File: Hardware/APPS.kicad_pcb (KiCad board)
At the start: 2 copper layers, 100 x 63 mm, 83 parts, among them J1 Screw_Terminal_01x02, J2 Screw_Terminal_01x03, J3 Screw_Terminal_01x03, J4 Conn_01x06_Male, J5 Screw_Terminal_01x02, J6 Conn_01x06_Male, J7 Screw_Terminal_01x02, K1 FINDER-30.22, Q1 BSS138, SW1 SW_Push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

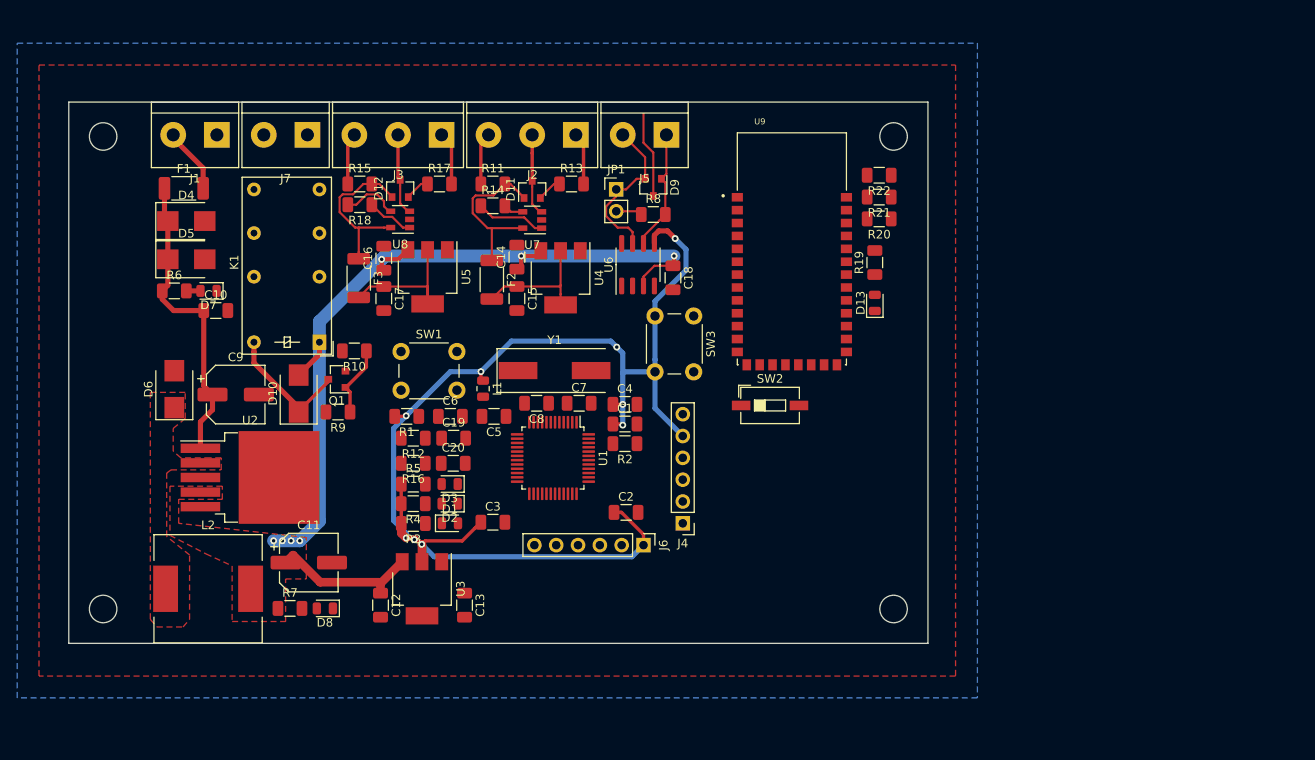
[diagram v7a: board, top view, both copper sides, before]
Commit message: Components labels placed
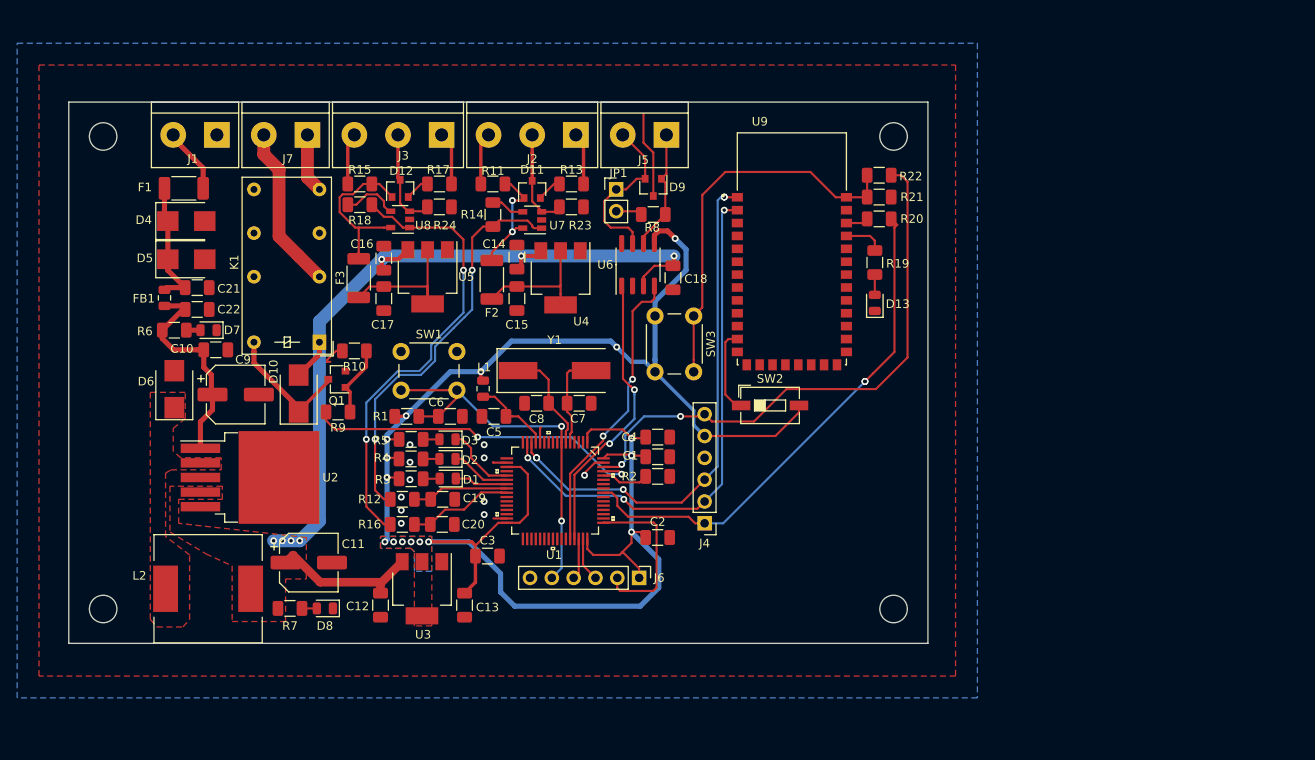
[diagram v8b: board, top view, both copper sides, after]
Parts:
- added C21: C_Small, Capacitor_SMD:C_1206_3216Metric, F.Cu at (87.0, 74.2)
- added C22: C_Small, Capacitor_SMD:C_1206_3216Metric, F.Cu at (87.0, 76.7)
- added FB1: Ferrite_Bead_Small, Inductor_SMD:L_0805_2012Metric, F.Cu at (83.2, 75.4)
- added R23: 100k, Resistor_SMD:R_1206_3216Metric, F.Cu at (130.6, 64.8)
- added R24: 100k, Resistor_SMD:R_1206_3216Metric, F.Cu at (115.2, 64.8)
- U1: value STM32F103C8Tx -> STM32L4P5RET6; footprint Package_QFP:LQFP-48_7x7mm_P0.5mm -> footprints:STM32L4P5RET6
- moved R16 7.22 mm to (110.9, 101.7)
- moved C19 7.22 mm to (115.6, 98.8)
- moved R12 7.22 mm to (110.9, 98.8)
- moved C20 7.22 mm to (115.5, 101.7)
- moved R2 5.39 mm to (140.6, 96.1)
- moved C1 5.39 mm to (140.6, 93.9)
- moved C4 5.39 mm to (140.6, 91.6)
- moved D3 5.21 mm to (116.1, 91.8)
- moved D1 5.21 mm to (116.2, 96.4), turned to 180 degrees
- moved D2 5.21 mm to (116.1, 94.1)
- moved R3 5.21 mm to (111.9, 96.4)
- moved R4 5.21 mm to (111.9, 94.1)
- moved R5 5.21 mm to (111.9, 91.8)
- moved C2 4.70 mm to (140.6, 103.3)
- moved C10 4.57 mm to (89.2, 81.4)
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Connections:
- C10 pad 1: +24V -> Net-(C10-Pad1)
- C9 pad 1: +24V -> Net-(C10-Pad1)
- R6 pad 1: +24V -> Net-(C10-Pad1)
- U1 pad 11: Ain0 -> Net-(U1-Pad11)
- U1 pad 12: Ain1 -> SW_GND
- U1 pad 13: Net-(U1-Pad13) -> 3V3_A
- U1 pad 14: Net-(U1-Pad14) -> BT_TX
- U1 pad 15: Led1 -> BT_RX
- U1 pad 16: Led2 -> Net-(U1-Pad16)
- U1 pad 17: Led3 -> Net-(U1-Pad17)
- U1 pad 18: Net-(U1-Pad18) -> SW_GND
- U1 pad 19: Net-(U1-Pad19) -> 3V3_SYS
- U1 pad 21: Net-(U1-Pad21) -> Led1
- U1 pad 22: Net-(U1-Pad22) -> Led2
- U1 pad 23: SW_GND -> Led3
- U1 pad 24: 3V3_SYS -> Ain0
- U1 pad 25: Net-(U1-Pad25) -> Ain1
- U1 pad 31: Net-(U1-Pad31) -> SW_GND
- U1 pad 32: CAN_RX -> 3V3_SYS
- U1 pad 33: CAN_TX -> Net-(U1-Pad33)
- U1 pad 34: SWDIO -> Net-(U1-Pad34)
- U1 pad 35: SW_GND -> Net-(U1-Pad35)
- U1 pad 36: 3V3_SYS -> Net-(U1-Pad36)
- U1 pad 37: SWCLK -> Net-(U1-Pad37)
- U1 pad 40: BT_LED -> Net-(U1-Pad40)
- U1 pad 42: BT_RX -> Net-(U1-Pad42)
- U1 pad 43: BT_TX -> Net-(U1-Pad43)
- U1 pad 44: Net-(R2-Pad2) -> CAN_RX
- U1 pad 45: EN_RELAY -> CAN_TX
- U1 pad 46: BT_KEY -> SWDIO
- U1 pad 8: SW_GND -> Net-(U1-Pad8)
- U1 pad 9: 3V3_A -> Net-(U1-Pad9)
- U2 pad 1: +24V -> Net-(C10-Pad1)
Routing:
- net BT_KEY: track 0.00 -> 65.8 mm, vias 0 -> 2
- net BT_RX: track 0.00 -> 61.6 mm, vias 0 -> 3
- net 3V3_SYS: track 145.6 -> 206.3 mm, vias 9 -> 16
- net BT_TX: track 0.00 -> 60.5 mm, vias 0 -> 5
- net BT_LED: track 0.00 -> 60.0 mm, vias 0 -> 2
- net Net-(R16-Pad2): track 5.50 -> 53.2 mm, vias 0 -> 2
- net Net-(R21-Pad2): track 0.00 -> 45.1 mm
- net NRST: track 0.00 -> 44.8 mm, vias 0 -> 2
- net EN_RELAY: track 0.00 -> 40.3 mm, vias 0 -> 2
- net Net-(R12-Pad2): track 8.15 -> 47.1 mm, vias 0 -> 2
- net CAN_RX: track 0.00 -> 34.1 mm, vias 0 -> 2
- net CAN_TX: track 0.00 -> 33.3 mm, vias 0 -> 2
- net Net-(C10-Pad1): track 0.00 -> 25.0 mm
- net +24V: track 35.7 -> 15.1 mm
- net SWCLK: track 0.00 -> 19.6 mm
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- added copper zone on B.Cu, net 3V3_SYS
- added copper zone on F.Cu, net 3V3_SYS
